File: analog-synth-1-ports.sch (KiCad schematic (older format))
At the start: 1 part

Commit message: Begin working on ports
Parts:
- added J?: PJ301M-12, symbol custom-components:PJ301M-12
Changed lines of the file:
@@
 EESchema Schematic File Version 4
+LIBS:analog-synth-1-cache
 EELAYER 26 0
 EELAYER END
@@
 	2800 2400 2250 2400
 Connection ~ 2250 2400
+$Comp
+L custom-components:PJ301M-12 J?
+U 1 1 5C870E3E
+P 4650 1950
+F 0 "J?" H 4656 2325 50  0000 C CNN
+F 1 "PJ301M-12" H 4656 2234 50  0000 C CNN
+F 2 "" H 4650 1950 50  0000 C CNN
+F 3 "" H 4650 1950 50  0000 C CNN
+	1    4650 1950
+	1    0    0    -1
+$EndComp
 $EndSCHEMATC

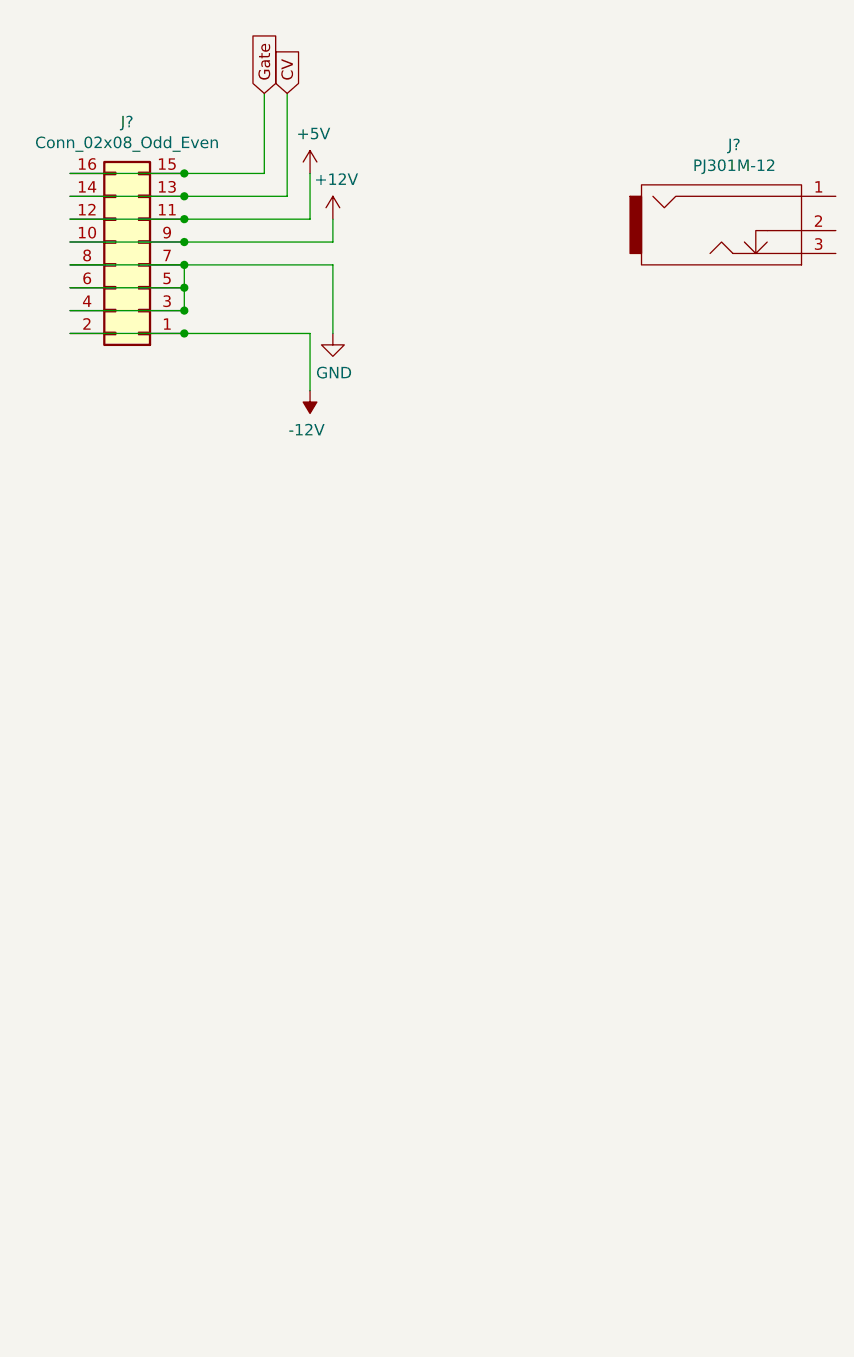
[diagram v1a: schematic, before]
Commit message: Add jacks
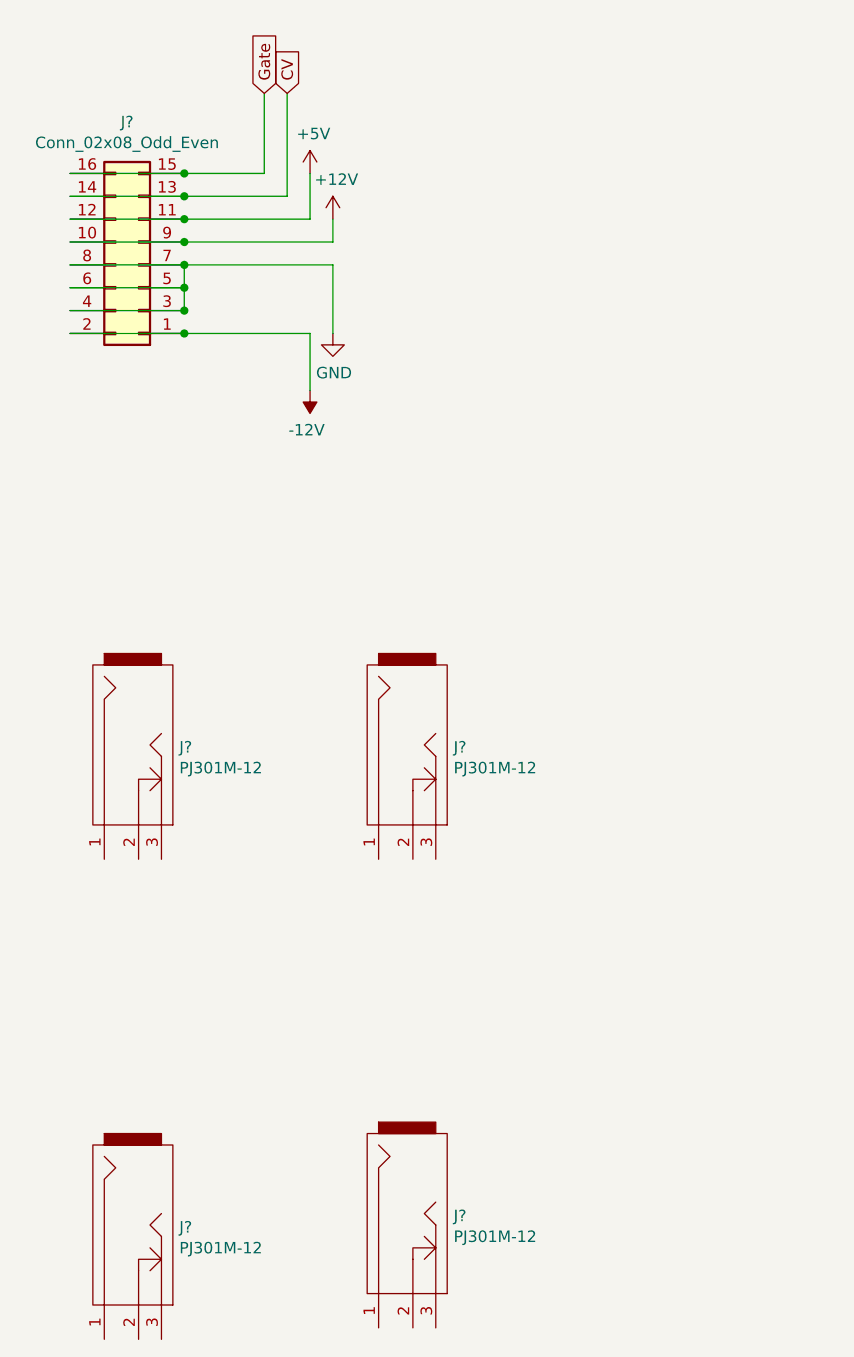
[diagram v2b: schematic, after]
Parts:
- removed J?: PJ301M-12, symbol custom-components:PJ301M-12
- added J? (x4): PJ301M-12, symbol custom-components:PJ301M-12
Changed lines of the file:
@@
 $Comp
 L custom-components:PJ301M-12 J?
-U 1 1 5C870E3E
-P 4650 1950
-F 0 "J?" H 4656 2325 50  0000 C CNN
-F 1 "PJ301M-12" H 4656 2234 50  0000 C CNN
-F 2 "" H 4650 1950 50  0000 C CNN
-F 3 "" H 4650 1950 50  0000 C CNN
-	1    4650 1950
-	1    0    0    -1
+U 1 1 5C87239F
+P 2050 4250
+F 0 "J?" V 2010 4072 50  0000 R CNN
+F 1 "PJ301M-12" V 2101 4072 50  0000 R CNN
+F 2 "" H 2050 4250 50  0000 C CNN
+F 3 "" H 2050 4250 50  0000 C CNN
+	1    2050 4250
+	0    -1   1    0
+$EndComp
+$Comp
+L custom-components:PJ301M-12 J?
+U 1 1 5C87271A
+P 3250 4250
+F 0 "J?" V 3210 4072 50  0000 R CNN
+F 1 "PJ301M-12" V 3301 4072 50  0000 R CNN
+F 2 "" H 3250 4250 50  0000 C CNN
+F 3 "" H 3250 4250 50  0000 C CNN
+	1    3250 4250
+	0    -1   1    0
+$EndComp
+$Comp
+L custom-components:PJ301M-12 J?
+U 1 1 5C8727CB
+P 2050 6350
+F 0 "J?" V 2010 6172 50  0000 R CNN
+F 1 "PJ301M-12" V 2101 6172 50  0000 R CNN
+F 2 "" H 2050 6350 50  0000 C CNN
+F 3 "" H 2050 6350 50  0000 C CNN
+	1    2050 6350
+	0    -1   1    0
+$EndComp
+$Comp
+L custom-components:PJ301M-12 J?
+U 1 1 5C872841
+P 3250 6300
+F 0 "J?" V 3210 6122 50  0000 R CNN
+F 1 "PJ301M-12" V 3301 6122 50  0000 R CNN
+F 2 "" H 3250 6300 50  0000 C CNN
+F 3 "" H 3250 6300 50  0000 C CNN
+	1    3250 6300
+	0    -1   1    0
 $EndComp
 $EndSCHEMATC

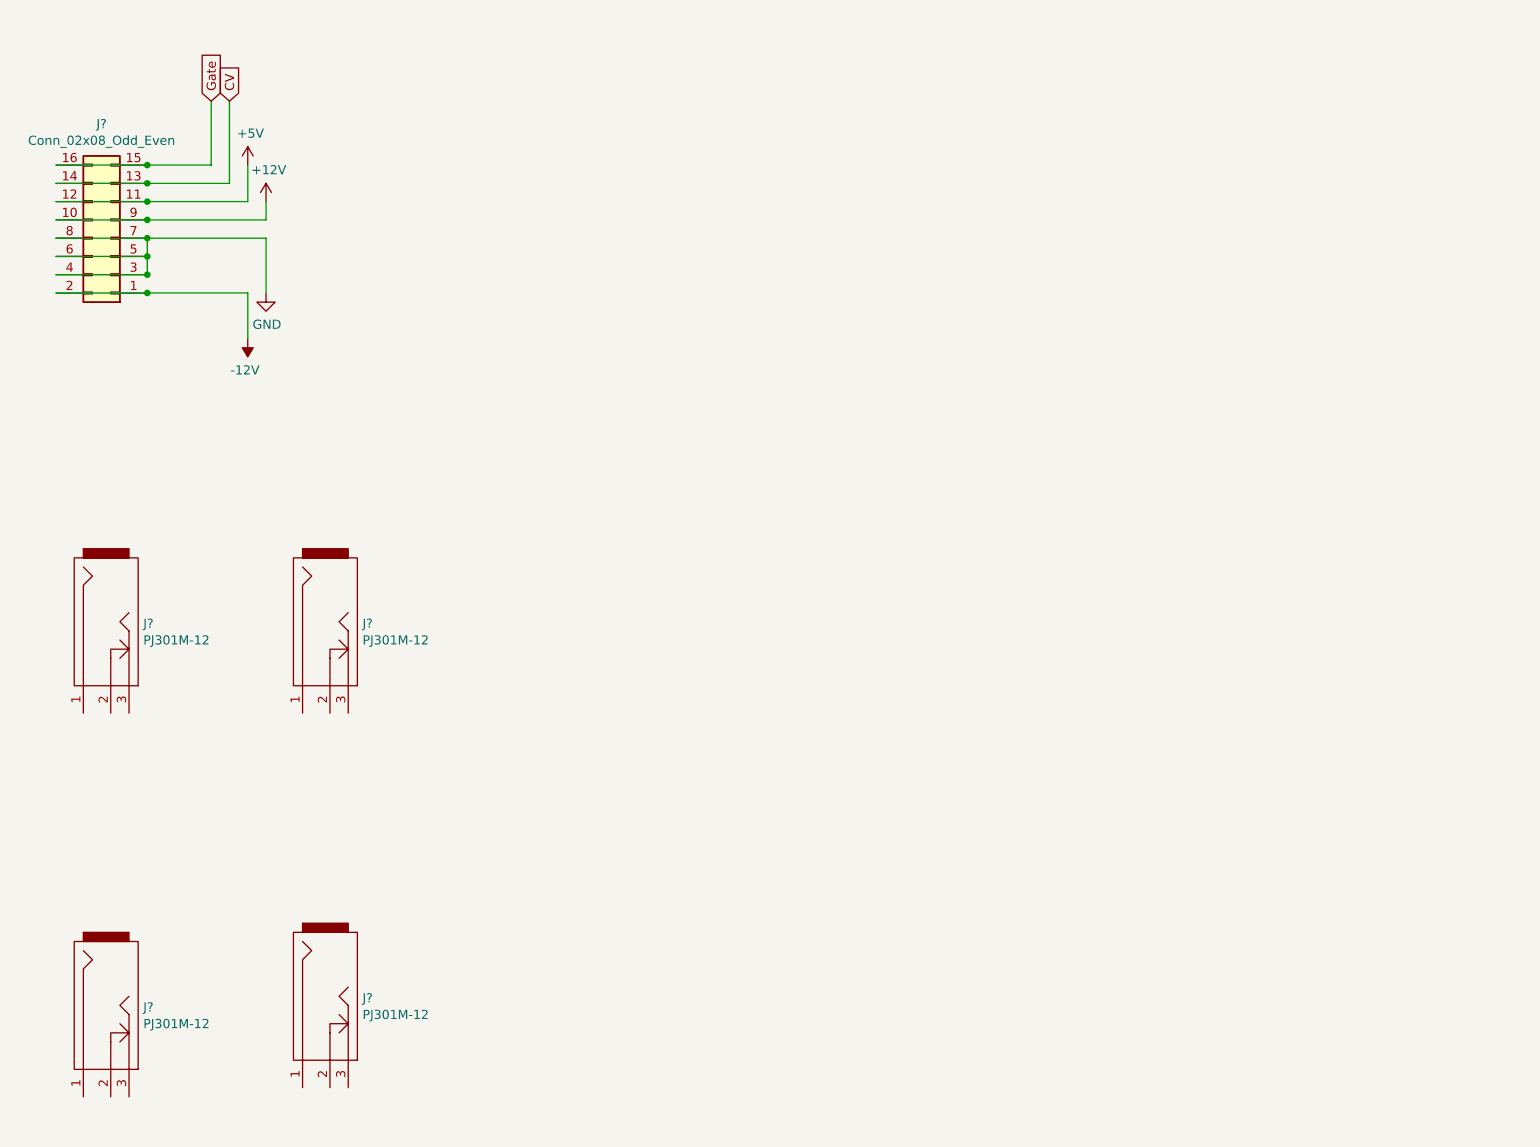
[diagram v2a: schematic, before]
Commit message: Add opamp buffers
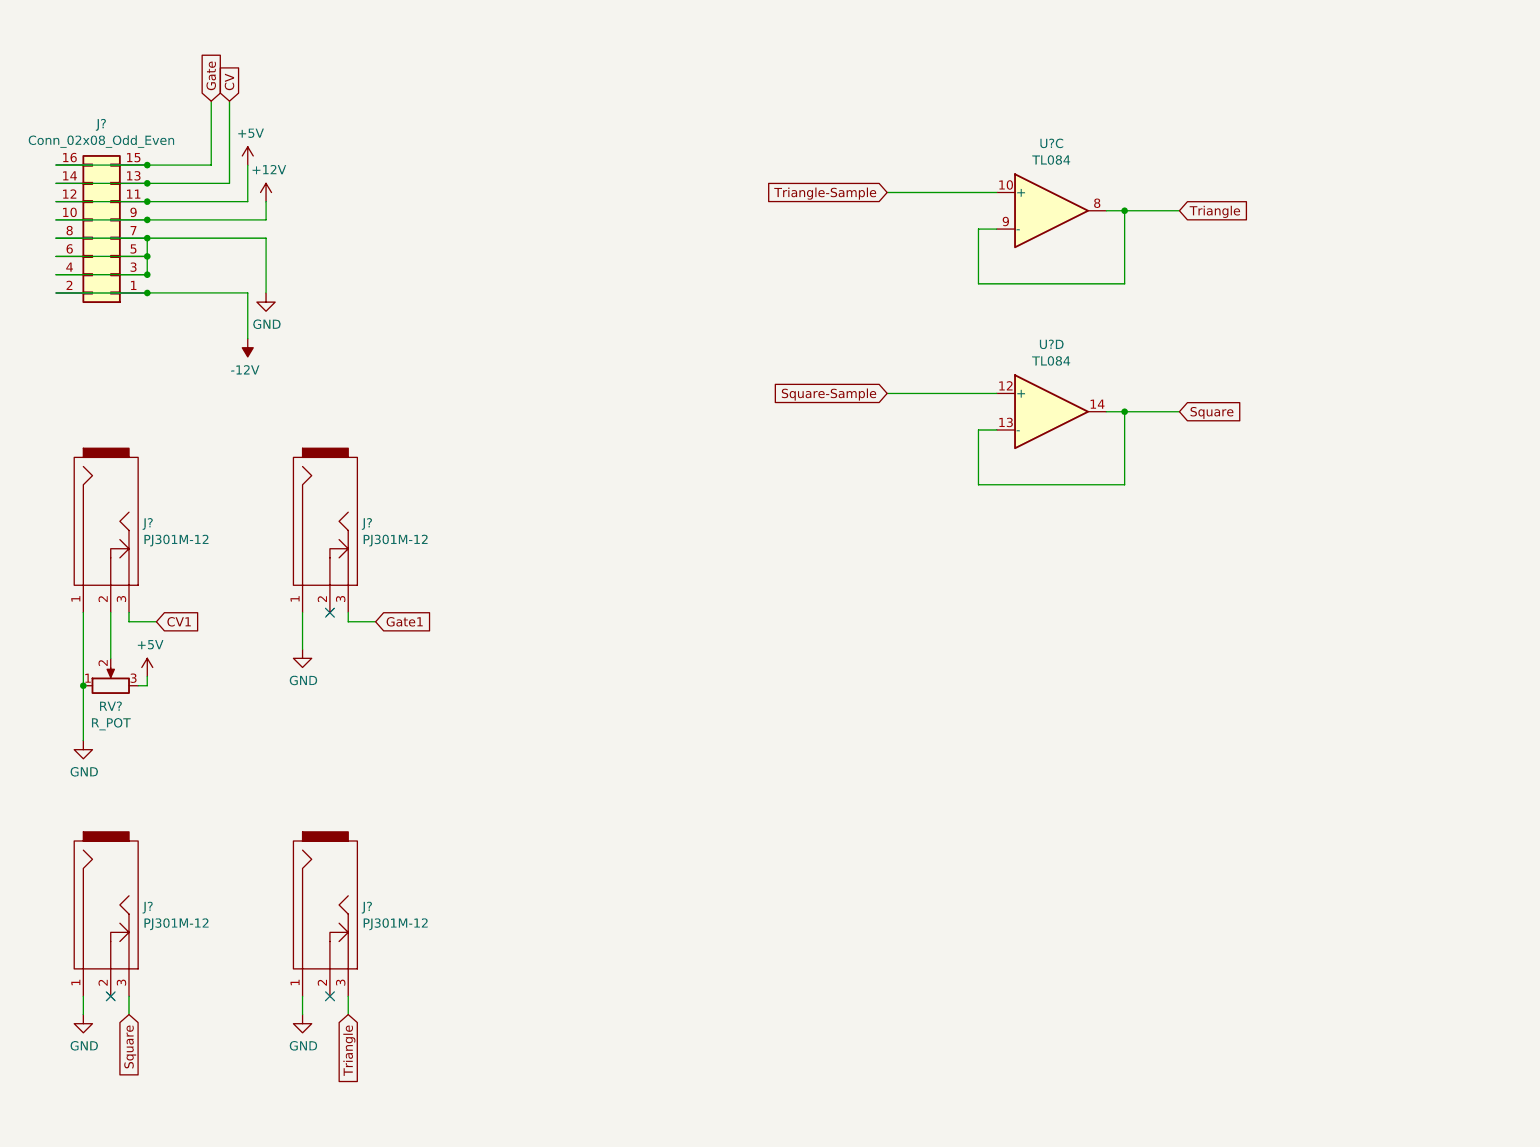
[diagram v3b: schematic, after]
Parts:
- added RV?: R_POT, symbol Device:R_POT
- added U? (x2): TL084, symbol Amplifier_Operational:TL084
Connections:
- net +5V: now also RV?.3
- net GND: now also J?.1, J?.1, J?.1, J?.1, RV?.1
- net at J?.2: now also RV?.2
- net CV1: now reaches J?.3
- net Gate1: now reaches J?.3
- net Square: now reaches J?.3
- net Square: now also U?.13 (-), U?.14
- net Triangle: now reaches J?.3
- net Triangle: now also U?.8, U?.9 (-)
- new net Square-Sample: U?.12 (+)
- new net Triangle-Sample: U?.10 (+)
- no-connect marks 0 -> 3
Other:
- moved on the sheet: J?
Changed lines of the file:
@@
 L custom-components:PJ301M-12 J?
 U 1 1 5C87239F
-P 2050 4250
-F 0 "J?" V 2010 4072 50  0000 R CNN
-F 1 "PJ301M-12" V 2101 4072 50  0000 R CNN
-F 2 "" H 2050 4250 50  0000 C CNN
-F 3 "" H 2050 4250 50  0000 C CNN
-	1    2050 4250
+P 2050 3700
+F 0 "J?" V 2010 3522 50  0000 R CNN
+F 1 "PJ301M-12" V 2101 3522 50  0000 R CNN
+F 2 "" H 2050 3700 50  0000 C CNN
+F 3 "" H 2050 3700 50  0000 C CNN
+	1    2050 3700
 	0    -1   1    0
 $EndComp
@@
 L custom-components:PJ301M-12 J?
 U 1 1 5C87271A
-P 3250 4250
-F 0 "J?" V 3210 4072 50  0000 R CNN
-F 1 "PJ301M-12" V 3301 4072 50  0000 R CNN
-F 2 "" H 3250 4250 50  0000 C CNN
-F 3 "" H 3250 4250 50  0000 C CNN
-	1    3250 4250
+P 3250 3700
+F 0 "J?" V 3210 3522 50  0000 R CNN
+F 1 "PJ301M-12" V 3301 3522 50  0000 R CNN
+F 2 "" H 3250 3700 50  0000 C CNN
+F 3 "" H 3250 3700 50  0000 C CNN
+	1    3250 3700
 	0    -1   1    0
 $EndComp
@@
 L custom-components:PJ301M-12 J?
 U 1 1 5C8727CB
-P 2050 6350
-F 0 "J?" V 2010 6172 50  0000 R CNN
-F 1 "PJ301M-12" V 2101 6172 50  0000 R CNN
-F 2 "" H 2050 6350 50  0000 C CNN
-F 3 "" H 2050 6350 50  0000 C CNN
-	1    2050 6350
+P 2050 5800
+F 0 "J?" V 2010 5622 50  0000 R CNN
+F 1 "PJ301M-12" V 2101 5622 50  0000 R CNN
+F 2 "" H 2050 5800 50  0000 C CNN
+F 3 "" H 2050 5800 50  0000 C CNN
+	1    2050 5800
 	0    -1   1    0
 $EndComp
@@
 L custom-components:PJ301M-12 J?
 U 1 1 5C872841
-P 3250 6300
-F 0 "J?" V 3210 6122 50  0000 R CNN
-F 1 "PJ301M-12" V 3301 6122 50  0000 R CNN
-F 2 "" H 3250 6300 50  0000 C CNN
-F 3 "" H 3250 6300 50  0000 C CNN
-	1    3250 6300
-	0    -1   1    0
-$EndComp
+P 3250 5800
+F 0 "J?" V 3210 5622 50  0000 R CNN
+F 1 "PJ301M-12" V 3301 5622 50  0000 R CNN
+F 2 "" H 3250 5800 50  0000 C CNN
+F 3 "" H 3250 5800 50  0000 C CNN
+	1    3250 5800
+	0    -1   1    0
+$EndComp
+$Comp
+L Device:R_POT RV?
+U 1 1 5C872CCA
+P 2050 4550
+F 0 "RV?" V 1936 4550 50  0000 C CNN
+F 1 "R_POT" V 1845 4550 50  0000 C CNN
+F 2 "" H 2050 4550 50  0001 C CNN
+F 3 "~" H 2050 4550 50  0001 C CNN
+	1    2050 4550
+	0    -1   -1   0
+$EndComp
+Wire Wire Line
+	2050 4400 2050 4150
+Wire Wire Line
+	1900 4150 1900 4550
+$Comp
+L power:GND #PWR?
+U 1 1 5C873F44
+P 1900 4850
+F 0 "#PWR?" H 1900 4600 50  0001 C CNN
+F 1 "GND" H 1905 4677 50  0000 C CNN
+F 2 "" H 1900 4850 50  0001 C CNN
+F 3 "" H 1900 4850 50  0001 C CNN
+	1    1900 4850
+	1    0    0    -1
+$EndComp
+Wire Wire Line
+	1900 4550 1900 4850
+Connection ~ 1900 4550
+$Comp
+L power:+5V #PWR?
+U 1 1 5C87478A
+P 2250 4500
+F 0 "#PWR?" H 2250 4350 50  0001 C CNN
+F 1 "+5V" H 2265 4673 50  0000 C CNN
+F 2 "" H 2250 4500 50  0001 C CNN
+F 3 "" H 2250 4500 50  0001 C CNN
+	1    2250 4500
+	1    0    0    -1
+$EndComp
+Wire Wire Line
+	2250 4500 2250 4550
+Wire Wire Line
+	2250 4550 2200 4550
+Text GLabel 2300 4200 2    50   Input ~ 0
+CV1
+Wire Wire Line
+	2300 4200 2150 4200
+Wire Wire Line
+	2150 4200 2150 4150
+NoConn ~ 3250 4150
+$Comp
+L power:GND #PWR?
+U 1 1 5C875167
+P 3100 4350
+F 0 "#PWR?" H 3100 4100 50  0001 C CNN
+F 1 "GND" H 3105 4177 50  0000 C CNN
+F 2 "" H 3100 4350 50  0001 C CNN
+F 3 "" H 3100 4350 50  0001 C CNN
+	1    3100 4350
+	1    0    0    -1
+$EndComp
+Wire Wire Line
+	3100 4350 3100 4150
+Text GLabel 3500 4200 2    50   Input ~ 0
+Gate1
+Wire Wire Line
+	3500 4200 3350 4200
+Wire Wire Line
+	3350 4200 3350 4150
+Text GLabel 2150 6350 3    50   Input ~ 0
+Square
+Wire Wire Line
+	2150 6350 2150 6250
+$Comp
+L power:GND #PWR?
+U 1 1 5C876B03
+P 1900 6350
+F 0 "#PWR?" H 1900 6100 50  0001 C CNN
+F 1 "GND" H 1905 6177 50  0000 C CNN
+F 2 "" H 1900 6350 50  0001 C CNN
+F 3 "" H 1900 6350 50  0001 C CNN
+	1    1900 6350
+	1    0    0    -1
+$EndComp
+Wire Wire Line
+	1900 6350 1900 6250
+NoConn ~ 2050 6250
+$Comp
+L power:GND #PWR?
+U 1 1 5C877B99
+P 3100 6350
+F 0 "#PWR?" H 3100 6100 50  0001 C CNN
+F 1 "GND" H 3105 6177 50  0000 C CNN
+F 2 "" H 3100 6350 50  0001 C CNN
+F 3 "" H 3100 6350 50  0001 C CNN
+	1    3100 6350
+	1    0    0    -1
+$EndComp
+Wire Wire Line
+	3100 6350 3100 6250
+NoConn ~ 3250 6250
+Text GLabel 3350 6350 3    50   Input ~ 0
+Triangle
+Wire Wire Line
+	3350 6350 3350 6250
+$Comp
+L Amplifier_Operational:TL084 U?
+U 3 1 5C878E0C
+P 7200 1950
+F 0 "U?" H 7200 2317 50  0000 C CNN
+F 1 "TL084" H 7200 2226 50  0000 C CNN
+F 2 "" H 7150 2050 50  0001 C CNN
+F 3 "http://www.ti.com/lit/ds/symlink/tl081.pdf" H 7250 2150 50  0001 C CNN
+	3    7200 1950
+	1    0    0    -1
+$EndComp
+$Comp
+L Amplifier_Operational:TL084 U?
+U 4 1 5C878EAE
+P 7200 3050
+F 0 "U?" H 7200 3417 50  0000 C CNN
+F 1 "TL084" H 7200 3326 50  0000 C CNN
+F 2 "" H 7150 3150 50  0001 C CNN
+F 3 "http://www.ti.com/lit/ds/symlink/tl081.pdf" H 7250 3250 50  0001 C CNN
+	4    7200 3050
+	1    0    0    -1
+$EndComp
+Wire Wire Line
+	6900 2050 6800 2050
+Wire Wire Line
+	6800 2050 6800 2350
+Wire Wire Line
+	6800 2350 7600 2350
+Wire Wire Line
+	7600 2350 7600 1950
+Wire Wire Line
+	7600 1950 7500 1950
+Wire Wire Line
+	6900 3150 6800 3150
+Wire Wire Line
+	6800 3150 6800 3450
+Wire Wire Line
+	6800 3450 7600 3450
+Wire Wire Line
+	7600 3450 7600 3050
+Wire Wire Line
+	7600 3050 7500 3050
+Text GLabel 6300 1850 0    50   Input ~ 0
+Triangle-Sample
+Text GLabel 6300 2950 0    50   Input ~ 0
+Square-Sample
+Wire Wire Line
+	6300 1850 6900 1850
+Wire Wire Line
+	6300 2950 6900 2950
+Text GLabel 7900 1950 2    50   Input ~ 0
+Triangle
+Wire Wire Line
+	7900 1950 7600 1950
+Connection ~ 7600 1950
+Text GLabel 7900 3050 2    50   Input ~ 0
+Square
+Wire Wire Line
+	7900 3050 7600 3050
+Connection ~ 7600 3050
 $EndSCHEMATC

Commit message: Add CV input amp
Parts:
- added R? (x2): R, symbol Device:R
- added RV?: R_POT_TRIM, symbol Device:R_POT_TRIM
- added U?: TL084, symbol Amplifier_Operational:TL084
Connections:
- net CV: now also R?.2
- net CV1: now also R?.2
- net GND: now also U?.10 (+)
- new net: R?.1, R?.1, RV?.3, U?.9 (-)
- new net VIN: RV?.1, RV?.2, U?.8
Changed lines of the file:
@@
 	7900 3050 7600 3050
 Connection ~ 7600 3050
+$Comp
+L Amplifier_Operational:TL084 U?
+U 3 1 5C87D386
+P 7200 5000
+F 0 "U?" H 7200 5367 50  0000 C CNN
+F 1 "TL084" H 7200 5276 50  0000 C CNN
+F 2 "" H 7150 5100 50  0001 C CNN
+F 3 "http://www.ti.com/lit/ds/symlink/tl081.pdf" H 7250 5200 50  0001 C CNN
+	3    7200 5000
+	1    0    0    -1
+$EndComp
+$Comp
+L Device:R_POT_TRIM RV?
+U 1 1 5C87DFED
+P 7150 5600
+F 0 "RV?" V 6943 5600 50  0000 C CNN
+F 1 "R_POT_TRIM" V 7034 5600 50  0000 C CNN
+F 2 "" H 7150 5600 50  0001 C CNN
+F 3 "~" H 7150 5600 50  0001 C CNN
+	1    7150 5600
+	0    1    1    0
+$EndComp
+Wire Wire Line
+	7300 5600 7600 5600
+Wire Wire Line
+	7600 5600 7600 5000
+Wire Wire Line
+	7600 5000 7500 5000
+Wire Wire Line
+	7000 5600 6800 5600
+Wire Wire Line
+	6800 5600 6800 5100
+Wire Wire Line
+	6800 5100 6900 5100
+Wire Wire Line
+	7150 5750 7600 5750
+Wire Wire Line
+	7600 5750 7600 5600
+Connection ~ 7600 5600
+$Comp
+L power:GND #PWR?
+U 1 1 5C880099
+P 6650 4800
+F 0 "#PWR?" H 6650 4550 50  0001 C CNN
+F 1 "GND" H 6655 4627 50  0000 C CNN
+F 2 "" H 6650 4800 50  0001 C CNN
+F 3 "" H 6650 4800 50  0001 C CNN
+	1    6650 4800
+	1    0    0    -1
+$EndComp
+Wire Wire Line
+	6900 4900 6800 4900
+Wire Wire Line
+	6800 4900 6800 4700
+Wire Wire Line
+	6800 4700 6650 4700
+Wire Wire Line
+	6650 4700 6650 4800
+$Comp
+L Device:R R?
+U 1 1 5C880E42
+P 6350 5100
+F 0 "R?" V 6143 5100 50  0000 C CNN
+F 1 "R" V 6234 5100 50  0000 C CNN
+F 2 "" V 6280 5100 50  0001 C CNN
+F 3 "~" H 6350 5100 50  0001 C CNN
+	1    6350 5100
+	0    1    1    0
+$EndComp
+$Comp
+L Device:R R?
+U 1 1 5C880EB3
+P 6350 5600
+F 0 "R?" V 6143 5600 50  0000 C CNN
+F 1 "R" V 6234 5600 50  0000 C CNN
+F 2 "" V 6280 5600 50  0001 C CNN
+F 3 "~" H 6350 5600 50  0001 C CNN
+	1    6350 5600
+	0    1    1    0
+$EndComp
+Wire Wire Line
+	6500 5100 6800 5100
+Connection ~ 6800 5100
+Wire Wire Line
+	6500 5600 6800 5600
+Connection ~ 6800 5600
+Text GLabel 6000 5100 0    50   Input ~ 0
+CV
+Wire Wire Line
+	6000 5100 6200 5100
+Text GLabel 6000 5600 0    50   Input ~ 0
+CV1
+Wire Wire Line
+	6000 5600 6200 5600
+Text GLabel 7800 5000 2    50   Input ~ 0
+VIN
+Wire Wire Line
+	7800 5000 7600 5000
+Connection ~ 7600 5000
 $EndSCHEMATC
